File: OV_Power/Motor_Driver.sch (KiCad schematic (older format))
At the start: 23 parts, among them CN1 CONN_HEADER_R_A_2POS_2.5MM, U3 LMC6772AIMX, U4 VNH5019ATR-E

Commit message: First cut at a placement study for the power board.
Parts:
- removed R28, R29: 4k7_0603_Chip_Resistor,_1%,_0.1W, Resistor_SMD:R_0603_1608Metric, symbol OpenVent:4k7_0603_Chip_Resistor,_1%,_0.1W
- CN1: footprint (none) -> OpenVent:53426-0210
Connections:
- wire segments 103 -> 99
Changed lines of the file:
@@
 Text Notes 8950 2600 0    60   ~ 0
 Mates with Molex cable assembly 151370201
-$Comp
-L OpenVent:3V3 #PWR017
-U 1 1 5F8DD12B
-P 3250 650
-F 0 "#PWR017" H 3250 650 50  0001 C CNN
-F 1 "3V3" H 3150 750 50  0000 C CNN
-F 2 "" H 3250 650 50  0001 C CNN
-F 3 "" H 3250 650 50  0001 C CNN
-	1    3250 650
-	1    0    0    -1
-$EndComp
 NoConn ~ 4750 1850
 NoConn ~ 4750 2150
@@
 Text GLabel 2250 1250 0    60   Output ~ 0
 nMOTOR-FAULT-B
-$Comp
-L OpenVent:3V3 #PWR018
-U 1 1 5F8DD12A
-P 3700 650
-F 0 "#PWR018" H 3700 650 50  0001 C CNN
-F 1 "3V3" H 3600 750 50  0000 C CNN
-F 2 "" H 3700 650 50  0001 C CNN
-F 3 "" H 3700 650 50  0001 C CNN
-	1    3700 650
-	1    0    0    -1
-$EndComp
 NoConn ~ 4750 2250
 $Comp
@@
 	2700 1450 2250 1450
 Wire Wire Line
-	2250 1250 3250 1250
-Wire Wire Line
-	2250 1150 3700 1150
-Wire Wire Line
 	3100 2050 4750 2050
 Wire Wire Line
@@
 Wire Wire Line
 	3100 1450 4750 1450
-Wire Wire Line
-	3250 1250 4750 1250
-Wire Wire Line
-	3250 1050 3250 1250
-Wire Wire Line
-	3700 1150 4750 1150
-Wire Wire Line
-	3700 1050 3700 1150
 Wire Wire Line
 	4350 2950 4750 2950
@@
 	10150 1200 10150 1350
 Connection ~ 2450 2050
-Connection ~ 3250 1250
-Connection ~ 3700 1150
 Connection ~ 4350 3750
 Connection ~ 4350 3150
@@
 F 0 "CN1" H 8900 1750 50  0000 L BNN
 F 1 "CONN_HEADER_R_A_2POS_2.5MM" H 8700 1950 50  0001 C CNN
-F 2 "" H 8700 1950 50  0001 C CNN
-F 3 "" H 8700 1950 50  0001 C CNN
+F 2 "OpenVent:53426-0210" H 8700 1950 50  0001 C CNN
+F 3 "https://www.molex.com/pdm_docs/sd/534260210_sd.pdf" H 8700 1950 50  0001 C CNN
 F 4 "Molex" H 8700 1950 50  0001 C CNN "Mfr"
-F 5 "0534260210" H 8700 1950 50  0001 C CNN "Mfr_PN"
+F 5 "0534260210" H 9000 2250 50  0000 C CNN "Mfr_PN"
 	1    8700 1950
 	1    0    0    1
-$EndComp
-$Comp
-L OpenVent:4k7_0603_Chip_Resistor,_1%,_0.1W R28
-U 1 1 5F8DD117
-P 3350 950
-F 0 "R28" V 3150 1150 50  0000 L TNN
-F 1 "4k7_0603_Chip_Resistor,_1%,_0.1W" V 3250 1150 50  0001 C CNN
-F 2 "Resistor_SMD:R_0603_1608Metric" H 3450 1010 50  0001 C CNN
-F 3 "" H 3450 1010 60  0001 C CNN
-F 4 "1%" V 1150 -1350 50  0001 C CNN "Tolerance"
-F 5 "4k7" V 3300 1250 50  0000 C CNN "Val"
-F 6 "0.1W" H 3350 950 50  0001 C CNN "Watt"
-	1    3350 950
-	0    -1   1    0
 $EndComp
 $Comp
@@
 	1    4750 2950
 	1    0    0    -1
-$EndComp
-$Comp
-L OpenVent:4k7_0603_Chip_Resistor,_1%,_0.1W R29
-U 1 1 5F8DD115
-P 3800 950
-F 0 "R29" V 3650 850 50  0000 L BNN
-F 1 "4k7_0603_Chip_Resistor,_1%,_0.1W" V 3750 900 50  0001 C CNN
-F 2 "Resistor_SMD:R_0603_1608Metric" H 3900 1010 50  0001 C CNN
-F 3 "" H 3900 1010 60  0001 C CNN
-F 4 "1%" V 1150 -1350 50  0001 C CNN "Tolerance"
-F 5 "4k7" V 3750 900 50  0000 C CNN "Val"
-F 6 "0.1W" H 3800 950 50  0001 C CNN "Watt"
-	1    3800 950
-	0    -1   1    0
 $EndComp
 $Comp
@@
 	1    0    0    -1
 $EndComp
+Wire Wire Line
+	2250 1250 4750 1250
+Wire Wire Line
+	2250 1150 4750 1150
 $EndSCHEMATC

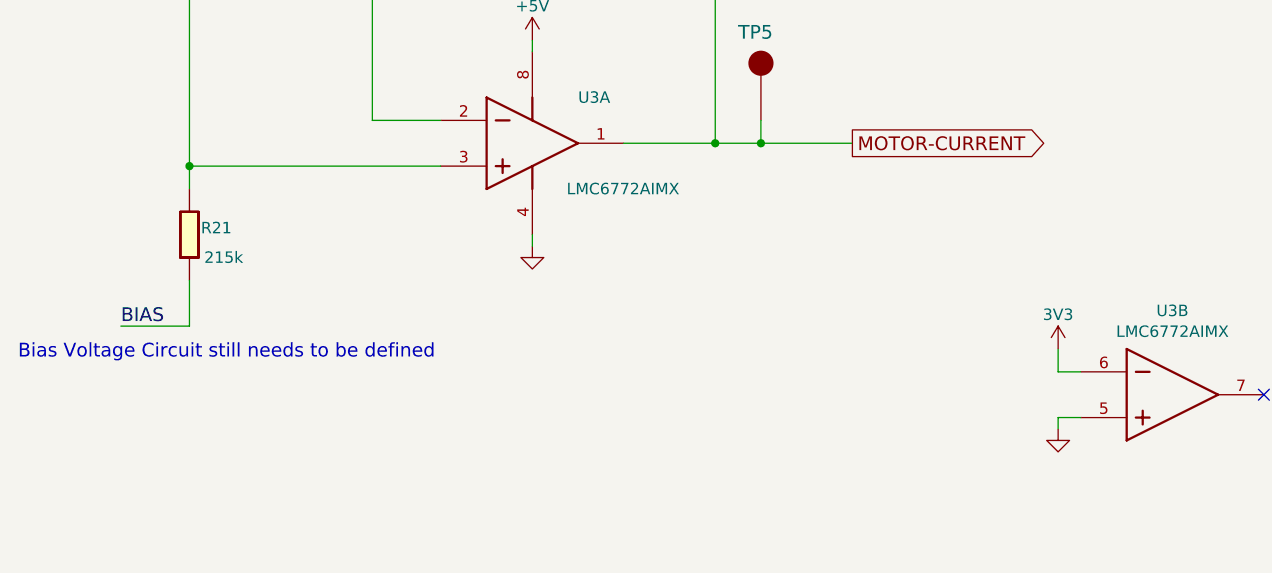
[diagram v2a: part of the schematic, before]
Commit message: Getting on with the placement of the power board, functional blocks are all grouped together, just need to fit them all in now.
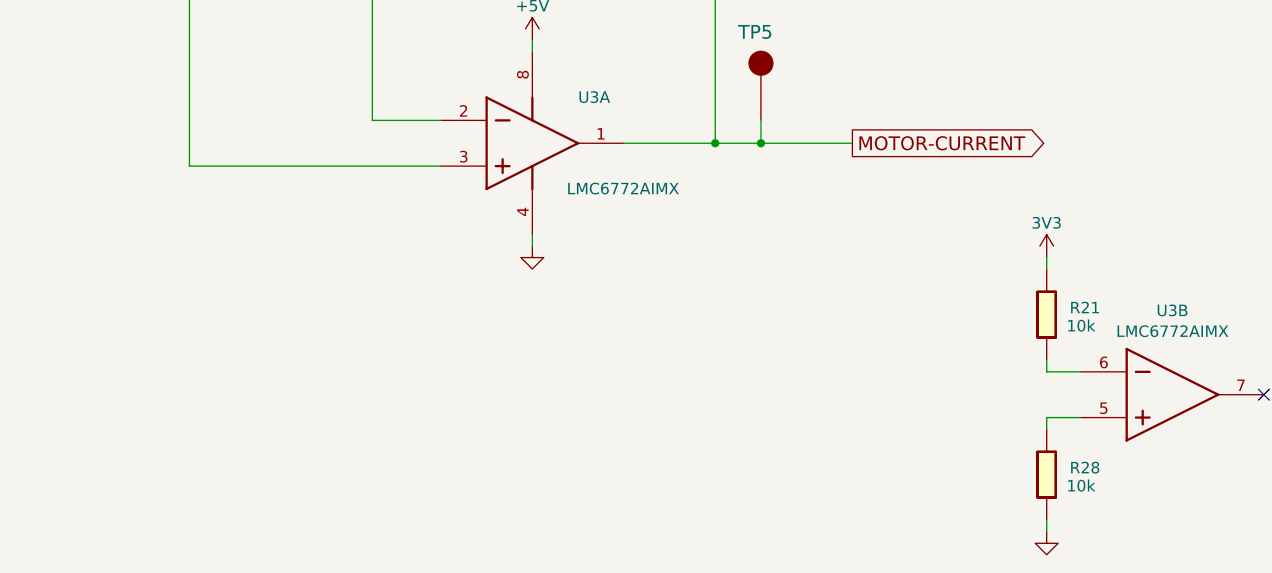
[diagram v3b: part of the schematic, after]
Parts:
- removed R21: 215k_0603_Chip_Resistor,_1%,_0.1W, Resistor_SMD:R_0603_1608Metric, symbol OpenVent:215k_0603_Chip_Resistor,_1%,_0.1W
- added R21, R28: 10k_0603_Chip_Resistor,_1%,_0.1W, Resistor_SMD:R_0603_1608Metric, symbol OpenVent:10k_0603_Chip_Resistor,_1%,_0.1W
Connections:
- net +3V3: now also R21.2; no longer U3.6 (INB-)
- net GND: now also R28.1; no longer U3.5 (INB+)
- new net: R28.2, U3.5 (INB+)
- new net: R21.1, U3.6 (INB-)
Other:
- note removed: "Bias Voltage Circuit still needs to be defined"
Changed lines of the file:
@@
 L OpenVent:3V3 #3V3_01
 U 1 1 5F8DD123
-P 5150 6850
-F 0 "#3V3_01" H 5150 6850 20  0001 C CNN
-F 1 "3V3" H 5150 7000 50  0000 C CNN
-F 2 "" H 5150 6850 70  0000 C CNN
-F 3 "" H 5150 6850 70  0000 C CNN
-	1    5150 6850
+P 5100 6450
+F 0 "#3V3_01" H 5100 6450 20  0001 C CNN
+F 1 "3V3" H 5100 6600 50  0000 C CNN
+F 2 "" H 5100 6450 70  0000 C CNN
+F 3 "" H 5100 6450 70  0000 C CNN
+	1    5100 6450
 	1    0    0    -1
 $EndComp
@@
 L OpenVent:GND #GND_015
 U 1 1 5F8DD122
-P 5150 7200
-F 0 "#GND_015" H 5150 7200 20  0001 C CNN
-F 1 "GND" H 5150 7050 50  0001 C CNN
-F 2 "" H 5150 7200 70  0000 C CNN
-F 3 "" H 5150 7200 70  0000 C CNN
-	1    5150 7200
+P 5100 7650
+F 0 "#GND_015" H 5100 7650 20  0001 C CNN
+F 1 "GND" H 5100 7500 50  0001 C CNN
+F 2 "" H 5100 7650 70  0000 C CNN
+F 3 "" H 5100 7650 70  0000 C CNN
+	1    5100 7650
 	1    0    0    -1
 $EndComp
@@
 	1    0    0    -1
 $EndComp
-Text Notes 600  6900 0    60   ~ 0
-Bias Voltage Circuit still needs to be defined
-Text Label 1050 6750 0    60   ~ 0
-BIAS
-Wire Wire Line
-	1350 6750 1350 6550
-Wire Wire Line
-	1050 6750 1350 6750
 Wire Wire Line
 	1350 6050 2450 6050
@@
 	1350 6050 1350 4350
 Wire Wire Line
-	1350 6150 1350 6050
-Wire Wire Line
 	2850 6350 2850 6400
 Wire Wire Line
@@
 Wire Wire Line
 	3850 5850 3850 5950
-Connection ~ 1350 6050
 Connection ~ 3650 5950
 Connection ~ 3850 5950
@@
 	0    1    1    0
 $EndComp
-$Comp
-L OpenVent:215k_0603_Chip_Resistor,_1%,_0.1W R21
-U 1 1 5F8DD0F5
-P 1450 6250
-F 0 "R21" V 1550 6200 50  0000 L BNN
-F 1 "215k_0603_Chip_Resistor,_1%,_0.1W" V 1650 6200 50  0001 C CNN
-F 2 "Resistor_SMD:R_0603_1608Metric" H 1750 6190 60  0001 C CNN
-F 3 "" H 1750 6190 60  0001 C CNN
-F 4 "1%" V 1150 -1650 50  0001 C CNN "Tolerance"
-F 5 "215k" V 1650 6300 50  0000 C CNN "Val"
-F 6 "0.1W" H 1450 6250 50  0001 C CNN "Watt"
-	1    1450 6250
-	0    1    1    0
-$EndComp
-Wire Wire Line
-	5250 6950 5150 6950
-Wire Wire Line
-	5150 6950 5150 6850
-Wire Wire Line
-	5250 7150 5150 7150
-Wire Wire Line
-	5150 7150 5150 7200
 Wire Wire Line
 	6600 1500 8700 1500
@@
 Wire Wire Line
 	2250 1150 4750 1150
+$Comp
+L OpenVent:10k_0603_Chip_Resistor,_1%,_0.1W R21
+U 1 1 5FCA17C3
+P 5000 6800
+F 0 "R21" V 5100 6600 50  0000 R TNN
+F 1 "10k_0603_Chip_Resistor,_1%,_0.1W" V 5000 6650 60  0001 C CNN
+F 2 "Resistor_SMD:R_0603_1608Metric" H 4900 6660 60  0001 C CNN
+F 3 "" H 4900 6660 60  0001 C CNN
+F 4 "1%" V 4900 1200 50  0001 C CNN "Tolerance"
+F 5 "10k" V 5050 6550 50  0000 C CNN "Val"
+F 6 "0.1W" H 5000 6800 50  0001 C CNN "Watt"
+	1    5000 6800
+	0    -1   -1   0
+$EndComp
+$Comp
+L OpenVent:10k_0603_Chip_Resistor,_1%,_0.1W R28
+U 1 1 5FCA572A
+P 5000 7500
+F 0 "R28" V 5100 7300 50  0000 R TNN
+F 1 "10k_0603_Chip_Resistor,_1%,_0.1W" V 5000 7350 60  0001 C CNN
+F 2 "Resistor_SMD:R_0603_1608Metric" H 4900 7360 60  0001 C CNN
+F 3 "" H 4900 7360 60  0001 C CNN
+F 4 "1%" V 4900 1900 50  0001 C CNN "Tolerance"
+F 5 "10k" V 5050 7250 50  0000 C CNN "Val"
+F 6 "0.1W" H 5000 7500 50  0001 C CNN "Watt"
+	1    5000 7500
+	0    -1   -1   0
+$EndComp
+Wire Wire Line
+	5250 6950 5100 6950
+Wire Wire Line
+	5100 6950 5100 6900
+Wire Wire Line
+	5100 6450 5100 6500
+Wire Wire Line
+	5250 7150 5100 7150
+Wire Wire Line
+	5100 7150 5100 7200
+Wire Wire Line
+	5100 7600 5100 7650
 $EndSCHEMATC

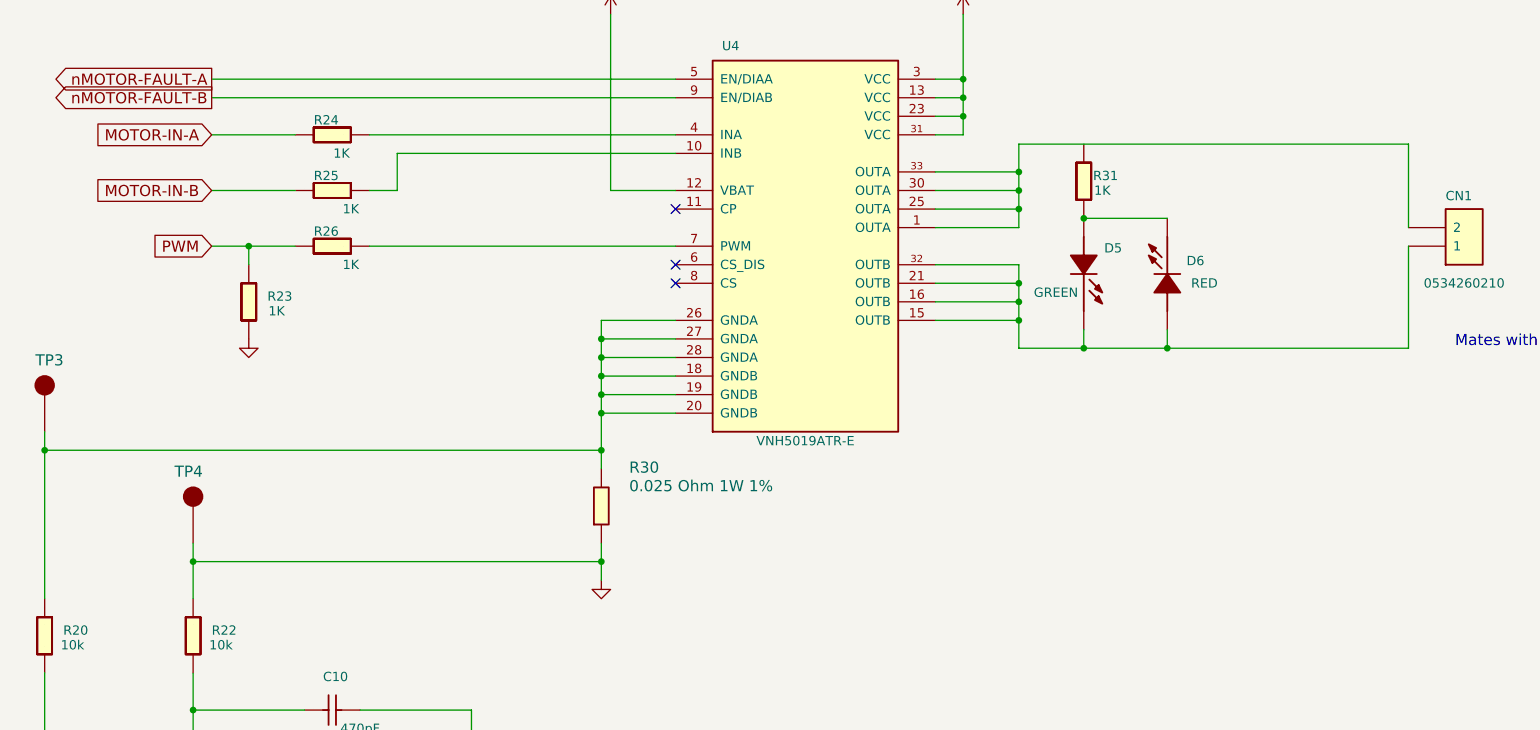
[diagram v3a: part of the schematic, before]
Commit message: Added two connectors for cooling fans, re-jigged the motor current sensing circuit a bit, still needs a bit of work there.
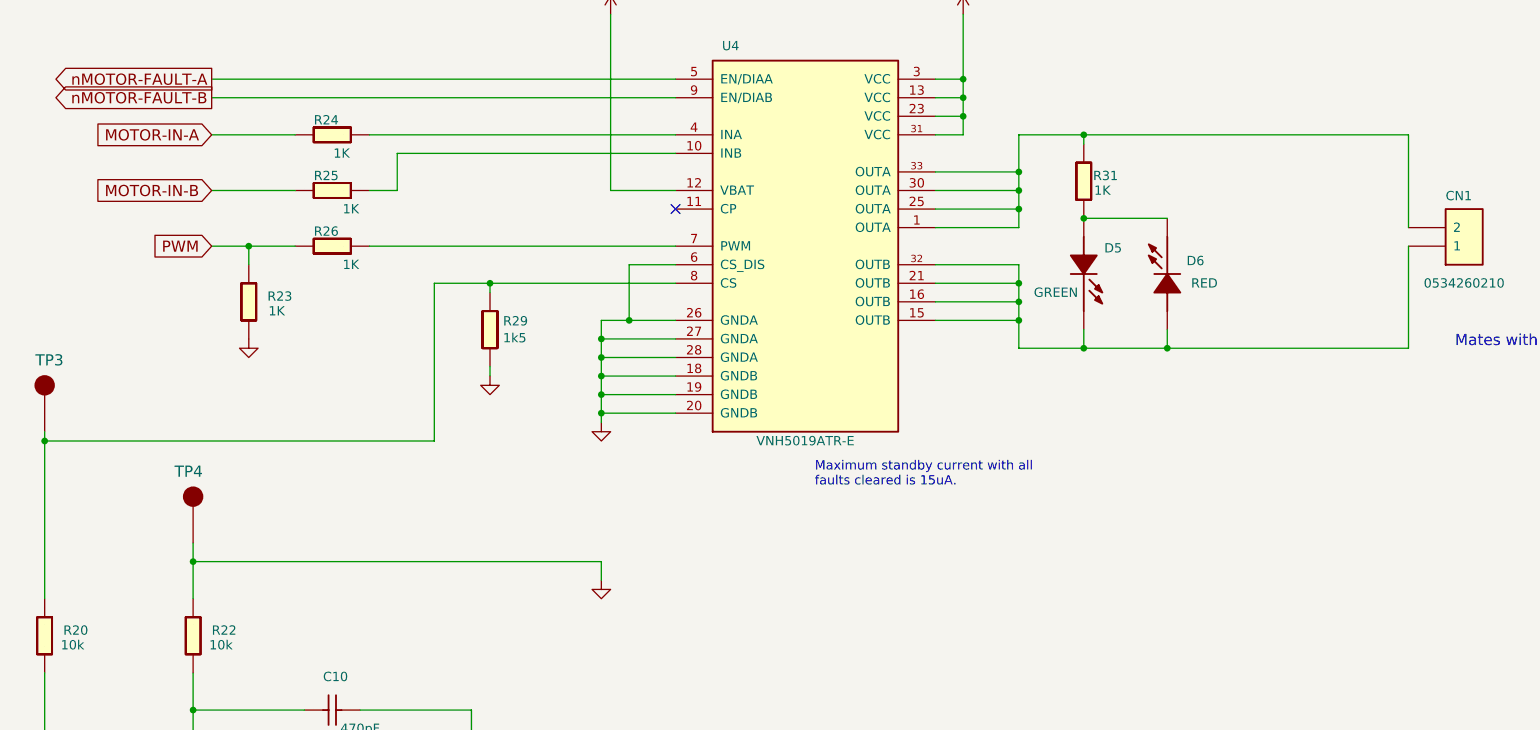
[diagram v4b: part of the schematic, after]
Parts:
- removed R30: 0.025 Ohm 1W 1%, Resistor_SMD:R_2010_5025Metric, symbol OpenVent:Resistor_2010_0.025OHM_sensing_1%_1W
- added R29: R_0603_1k5_0.1W_1%, Resistor_SMD:R_0603_1608Metric, symbol OpenVent:R_0603_1k5_0.1W_1%
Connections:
- net GND: now also U4.18 (GNDB), U4.19 (GNDB), U4.20 (GNDB), U4.26 (GNDA), U4.27 (GNDA), U4.28 (GNDA), U4.6 (CS_DIS), R29.2
- net at R31.1: now also CN1.2, U4.1 (OUTA), U4.25 (OUTA), U4.30 (OUTA), U4.33 (OUTA)
- net at U4.8 (CS): now also R20.2, TP3.1, R29.1
- no-connect marks 4 -> 2
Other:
- note added: "Maximum standby current with all\nfaults cleared is 15uA."
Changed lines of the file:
@@
 Mates with Molex cable assembly 151370201
 NoConn ~ 4750 1850
-NoConn ~ 4750 2150
 Text GLabel 2250 1150 0    60   Output ~ 0
 nMOTOR-FAULT-A
 Text GLabel 2250 1250 0    60   Output ~ 0
 nMOTOR-FAULT-B
-NoConn ~ 4750 2250
 $Comp
 L OpenVent:GND #GND_014
@@
 	4350 2950 4750 2950
 Wire Wire Line
-	4350 3150 4350 2950
-Wire Wire Line
-	4350 3250 4350 3150
-Wire Wire Line
 	4350 2850 4750 2850
 Wire Wire Line
@@
 	4350 2450 4350 2550
 Wire Wire Line
-	4750 2450 4350 2450
+	4750 2450 4500 2450
 Wire Wire Line
 	4400 1750 4750 1750
@@
 	6600 1650 6600 1750
 Wire Wire Line
-	6600 1500 6600 1650
-Wire Wire Line
-	8700 1950 8700 1500
-Wire Wire Line
 	6300 1350 6300 1450
 Wire Wire Line
@@
 Wire Wire Line
 	4350 3750 4350 3850
-Wire Wire Line
-	4350 3650 4350 3750
 Wire Wire Line
 	4350 2850 4350 2950
@@
 	10150 1200 10150 1350
 Connection ~ 2450 2050
-Connection ~ 4350 3750
-Connection ~ 4350 3150
-Connection ~ 4350 2950
 Connection ~ 4350 2850
 Connection ~ 4350 2750
@@
 	1    2800 1950
 	1    0    0    -1
-$EndComp
-$Comp
-L OpenVent:Resistor_2010_0.025OHM_sensing_1%_1W R30
-U 1 1 5F8DD0FA
-P 4250 3550
-F 0 "R30" V 4522 3300 60  0000 R TNN
-F 1 "0.025 Ohm 1W 1%" V 4422 3300 60  0000 R TNN
-F 2 "Resistor_SMD:R_2010_5025Metric" H 4422 3300 60  0001 C CNN
-F 3 "" H 4422 3300 60  0001 C CNN
-F 4 "WSL2010R0250FEA18" H 4250 3550 50  0001 C CNN "Mfr_PN"
-F 5 "Vishay Dale" H 4250 3550 50  0001 C CNN "Mfr"
-F 6 "1%" H 4250 3550 50  0001 C CNN "Tolerance"
-F 7 "0.025Ohm" H 4250 3550 50  0001 C CNN "Val"
-F 8 "1.0W" H 4250 3550 50  0001 C CNN "Watt"
-	1    4250 3550
-	0    -1   -1   0
 $EndComp
 $Comp
@@
 	2450 2050 2450 2150
 Wire Wire Line
-	1350 3150 4350 3150
-Wire Wire Line
-	1350 3950 1350 3150
-Wire Wire Line
 	2150 4550 2150 5050
 Wire Wire Line
@@
 	3650 5050 3650 4550
 Wire Wire Line
-	1350 3150 1350 3050
-Wire Wire Line
 	2150 3750 2150 3650
-Connection ~ 1350 3150
 Connection ~ 2150 5050
 Connection ~ 2150 4550
@@
 $EndComp
 Wire Wire Line
-	6600 1500 8700 1500
+	6600 1450 6950 1450
 $Comp
 L OpenVent:1000uF_25V_Aluminium_SMD_Capacitor,_20% C12
@@
 Wire Wire Line
 	5100 7600 5100 7650
+Wire Wire Line
+	6600 1450 6600 1650
+Wire Wire Line
+	8700 1450 8700 1950
+Wire Wire Line
+	6950 1500 6950 1450
+Connection ~ 6950 1450
+Wire Wire Line
+	6950 1450 8700 1450
+Text Notes 5500 3350 0    50   ~ 0
+Maximum standby current with all\nfaults cleared is 15uA.
+Wire Wire Line
+	1350 3050 1350 3100
+$Comp
+L OpenVent:GND #GND_020
+U 1 1 5FCEF3B0
+P 4350 3000
+F 0 "#GND_020" H 4350 3000 20  0001 C CNN
+F 1 "GND" H 4350 2930 50  0001 C CNN
+F 2 "" H 4350 3000 70  0000 C CNN
+F 3 "" H 4350 3000 70  0000 C CNN
+	1    4350 3000
+	1    0    0    -1
+$EndComp
+Wire Wire Line
+	4350 3000 4350 2950
+Connection ~ 4350 2950
+Wire Wire Line
+	4750 2150 4500 2150
+Wire Wire Line
+	4500 2150 4500 2450
+Connection ~ 4500 2450
+Wire Wire Line
+	4500 2450 4350 2450
+$Comp
+L OpenVent:R_0603_1k5_0.1W_1% R29
+U 1 1 5FCFA3BC
+P 3850 2400
+F 0 "R29" V 3904 2370 50  0000 L CNN
+F 1 "R_0603_1k5_0.1W_1%" H 3850 2400 50  0001 C CNN
+F 2 "Resistor_SMD:R_0603_1608Metric" H 3850 2400 60  0001 C CNN
+F 3 "" H 3850 2400 50  0001 C CNN
+F 4 "1k5" V 3995 2370 50  0000 L CNN "Val"
+F 5 "1%" H 3850 2400 50  0001 C CNN "Tolerance"
+F 6 "0.1W" H 3850 2400 50  0001 C CNN "Watt"
+	1    3850 2400
+	0    1    1    0
+$EndComp
+Wire Wire Line
+	4750 2250 3750 2250
+Wire Wire Line
+	3750 2250 3750 2300
+$Comp
+L OpenVent:GND #GND_019
+U 1 1 5FCFE3D6
+P 3750 2750
+F 0 "#GND_019" H 3750 2750 20  0001 C CNN
+F 1 "GND" H 3750 2680 50  0001 C CNN
+F 2 "" H 3750 2750 70  0000 C CNN
+F 3 "" H 3750 2750 70  0000 C CNN
+	1    3750 2750
+	1    0    0    -1
+$EndComp
+Wire Wire Line
+	3750 2750 3750 2700
+Wire Wire Line
+	3750 2250 3450 2250
+Wire Wire Line
+	3450 2250 3450 3100
+Wire Wire Line
+	3450 3100 1350 3100
+Connection ~ 3750 2250
+Connection ~ 1350 3100
+Wire Wire Line
+	1350 3100 1350 3950
 $EndSCHEMATC
